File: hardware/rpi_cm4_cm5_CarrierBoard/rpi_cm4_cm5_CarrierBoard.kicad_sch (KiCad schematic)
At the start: 0 parts

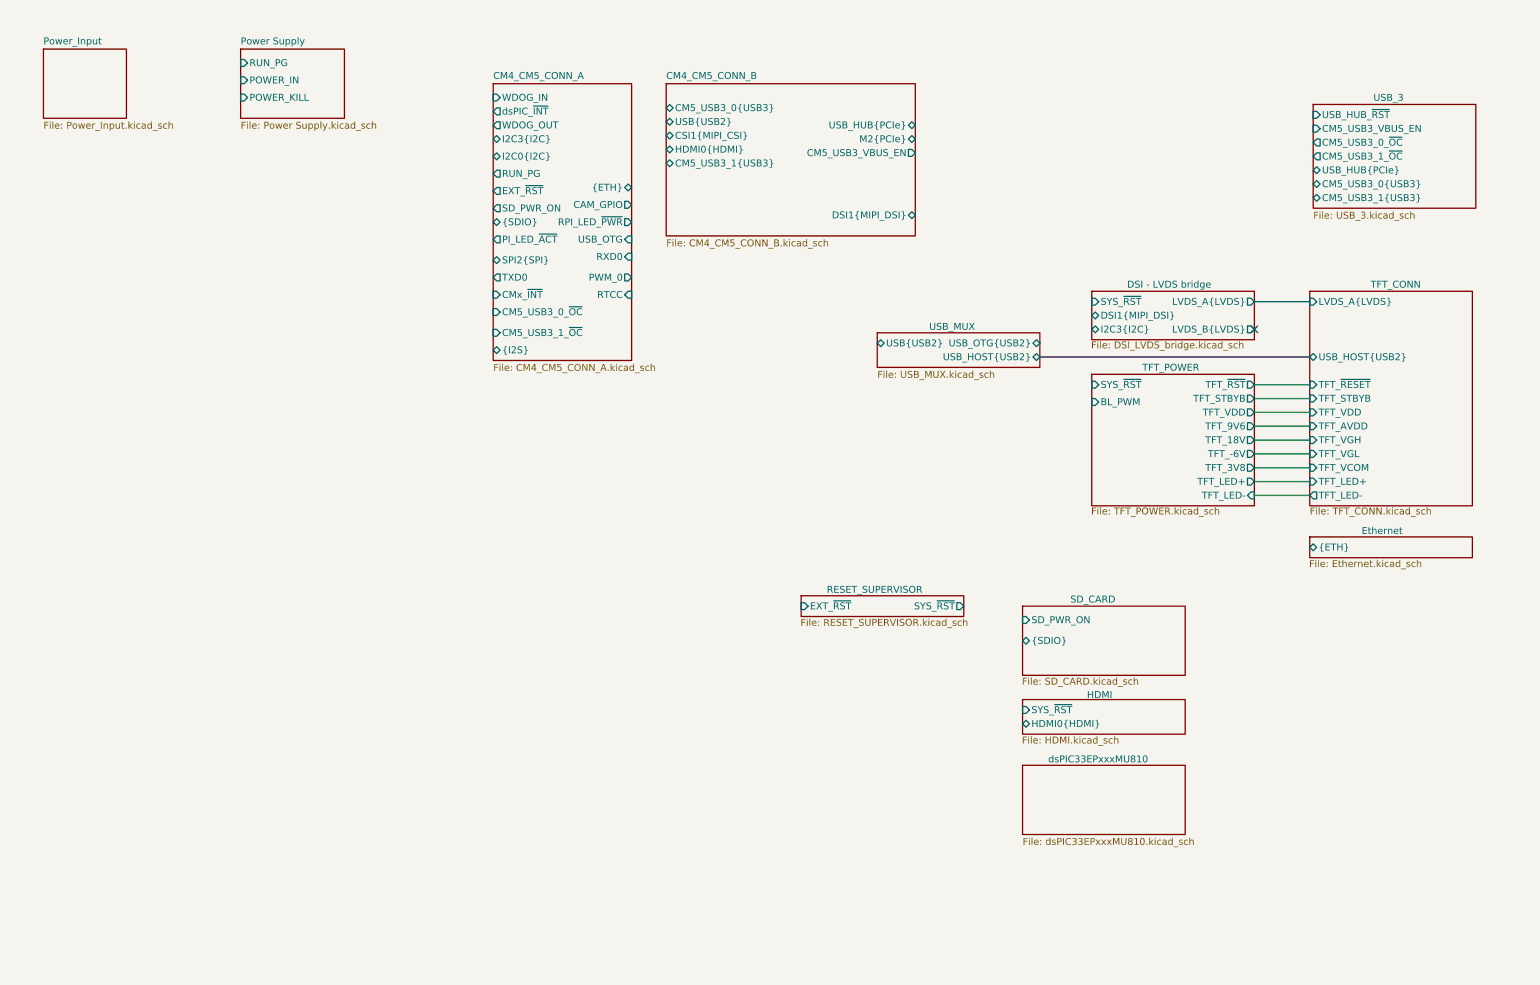
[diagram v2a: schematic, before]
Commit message: Significant update to schematics Add codec, Mikrobus, PIC32A Add power table, design notes for pinmux Add datasheets
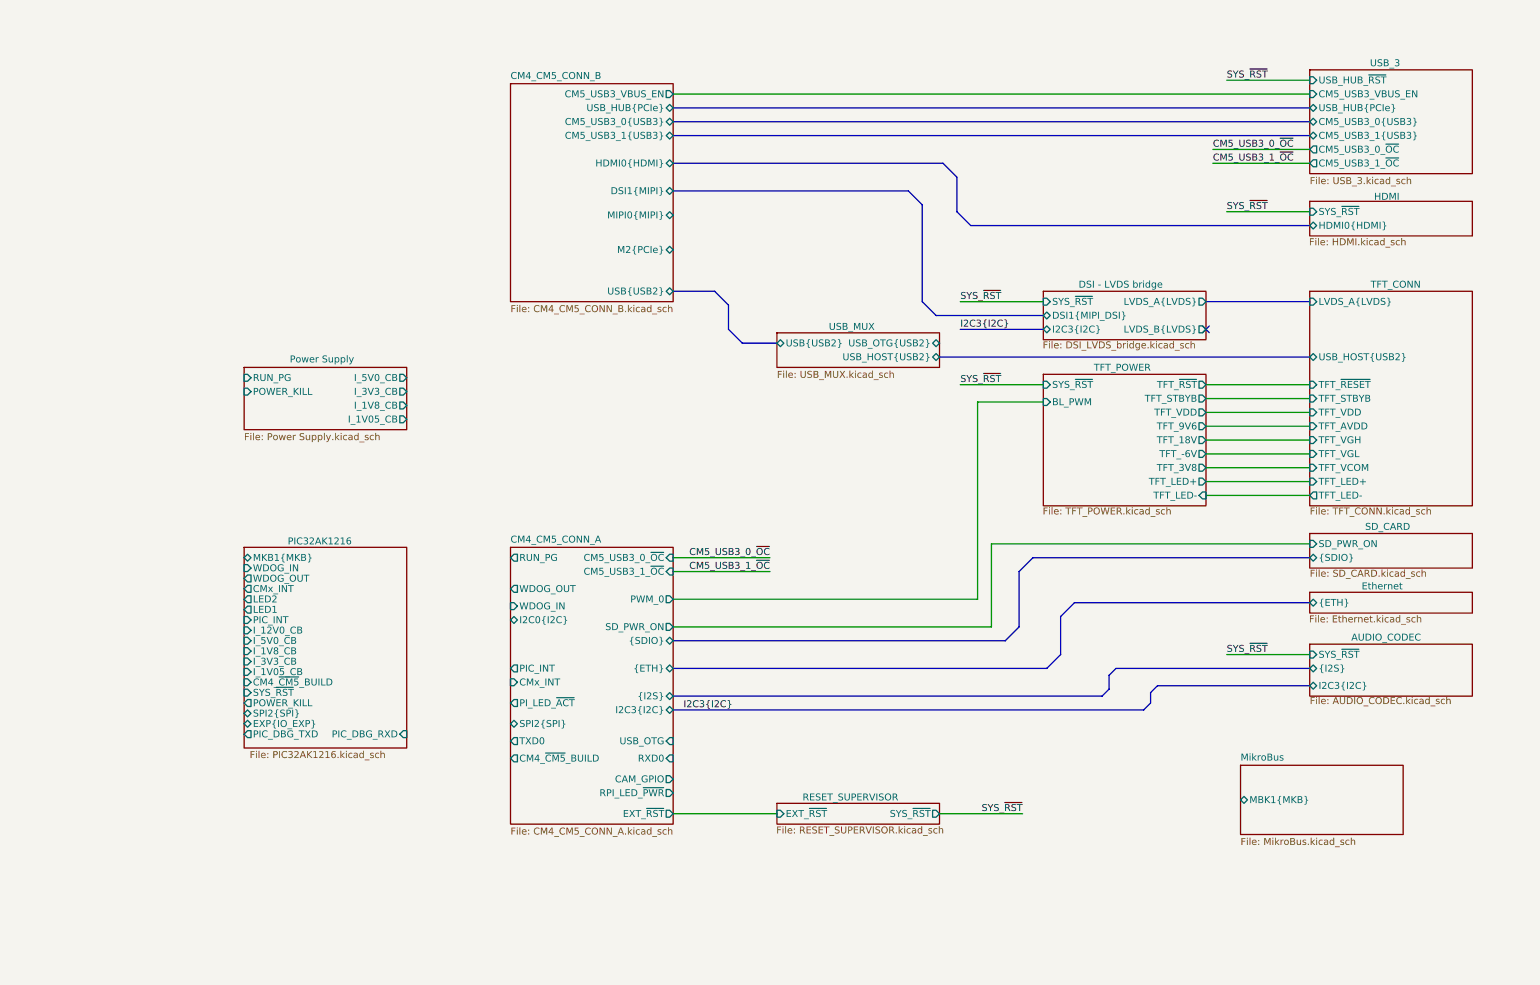
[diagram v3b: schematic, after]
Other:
- sheet dsPIC33EPxxxMU810 renamed PIC32AK1216
- removed sheet Power_Input
- added sheet AUDIO_CODEC (AUDIO_CODEC.kicad_sch)
- added sheet MikroBus (MikroBus.kicad_sch)
- sheet CM4_CM5_CONN_A ports: added CM4_~{CM5}_BUILD, CMx_INT, PIC_INT; removed CMx_~{INT}, RTCC, dsPIC_~{INT}
- sheet CM4_CM5_CONN_B ports: added DSI1{MIPI}, MIPI0{MIPI}; removed CSI1{MIPI_CSI}, DSI1{MIPI_DSI}
- sheet PIC32AK1216: file dsPIC33EPxxxMU810.kicad_sch -> PIC32AK1216.kicad_sch
- sheet PIC32AK1216 ports: added CM4_~{CM5}_BUILD, CMx_INT, EXP{IO_EXP}, I_12V0_CB, I_1V05_CB, I_1V8_CB, I_3V3_CB, I_5V0_CB, LED1, LED2, MKB1{MKB}, PIC_DBG_RXD, PIC_DBG_TXD, PIC_INT, POWER_KILL, SPI2{SPI}, SYS_~{RST}, WDOG_IN, WDOG_OUT; removed none
- sheet Power Supply ports: added I_1V05_CB, I_1V8_CB, I_3V3_CB, I_5V0_CB; removed POWER_IN

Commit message: Slight update to hierarchical top sheet
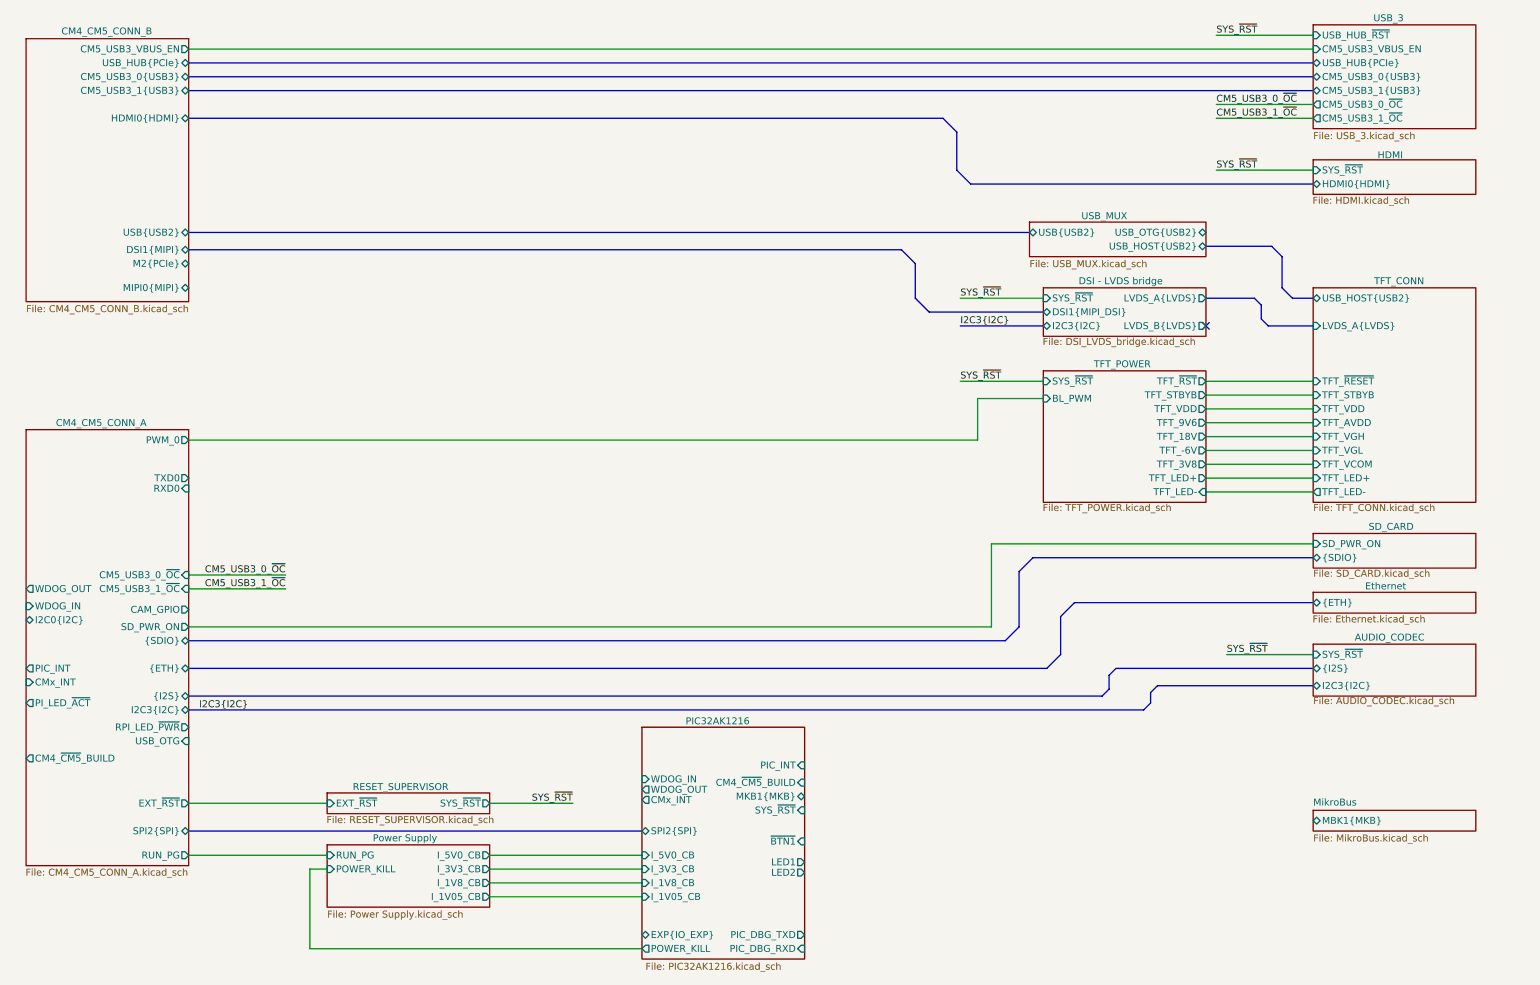
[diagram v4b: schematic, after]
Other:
- sheet PIC32AK1216 ports: added ~{BTN1}; removed I_12V0_CB

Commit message: Preliminary completion of RPI CMx schematics Cleaned up hierarchical root page
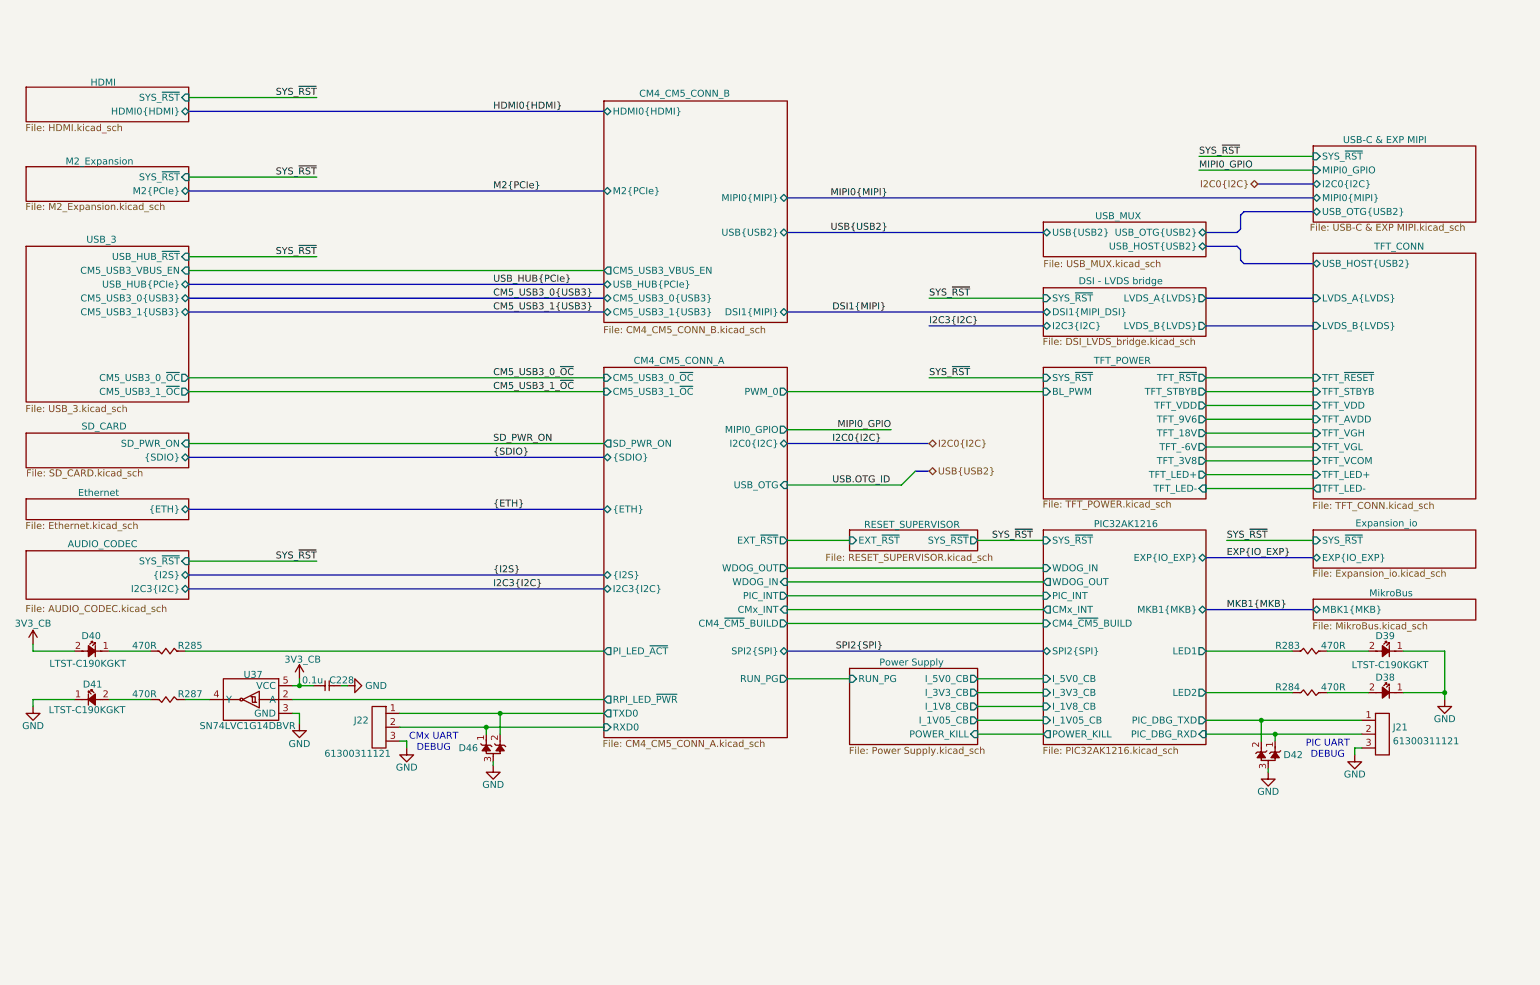
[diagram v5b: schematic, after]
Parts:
- added C228: 0.1u, footprint:CAP_NONPOL_0402, symbol KicadCompDb:Capacitors/CAP_CER_SMT_00001
- added D38, D39, D40, D41: LTST-C190KGKT, footprint:LED_0603, symbol KicadCompDb:Diodes/DIODE_00007
- added D42, D46: D1213A-02SOL-7, footprint:SOT-23-3, symbol KicadCompDb:ESD Diodes/ESD_DIODE_00002
- added J21, J22: 61300311121, footprint:HEADER_3P_2_54MM, symbol KicadCompDb:Connector/CONN_00001
- added R283, R284, R285, R287: 470R, footprint:RES_0402, symbol KicadCompDb:Resistors/RES_SMT_00019
- added U37: SN74LVC1G14DBVR, footprint:SOT-23-5, symbol KicadCompDb:Logic/LOGIC_00003
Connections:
- net CM4_CM5_CONN_A/PI_LED_~{ACT}: now also R285.1
- net CM4_CM5_CONN_A/RPI_LED_~{PWR}: now also U37.2 (A)
- net CM4_CM5_CONN_A/RXD0: now also D46.1, J22.2
- net CM4_CM5_CONN_A/TXD0: now also D46.2 (A), J22.1
- net PIC32AK1216/LED1: now also R283.1
- net PIC32AK1216/LED2: now also R284.1
- net PIC32AK1216/PIC_DBG_RXD: now also D42.1, J21.2
- net PIC32AK1216/PIC_DBG_TXD: now also D42.2 (A), J21.1
- new net: D39.2 (A), R283.2
- new net: D41.2 (A), R287.2
- new net: R287.1, U37.4 (Y)
- new net: D40.1 (K), R285.2
- new net: D38.2 (A), R284.2
- new net 3V3_CB: C228.2, D40.2 (A), U37.5 (VCC)
- new net GND: C228.1, D38.1 (K), D39.1 (K), D41.1 (K), D42.3 (GND), D46.3 (GND), J21.3, J22.3, U37.3 (GND)
- no-connect marks 1 -> 0
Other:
- added sheet Expansion_io (Expansion_io.kicad_sch)
- added sheet M2_Expansion (M2_Expansion.kicad_sch)
- added sheet USB-C & EXP MIPI (USB-C & EXP MIPI.kicad_sch)
- sheet CM4_CM5_CONN_A ports: added MIPI0_GPIO; removed CAM_GPIO
- sheet PIC32AK1216 ports: added none; removed ~{BTN1}
- sheet TFT_CONN ports: added LVDS_B{LVDS}; removed none
- note added: "CMx UART DEBUG"
- note added: "PIC UART DEBUG"

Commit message: Add preliminary BOM and preliminary .pdf schmematics Add BOM option for I2C control of ILI2132A for CapTouch HMI Add BOM options and DNP / 0R resistors for CM4 - CM5 build options
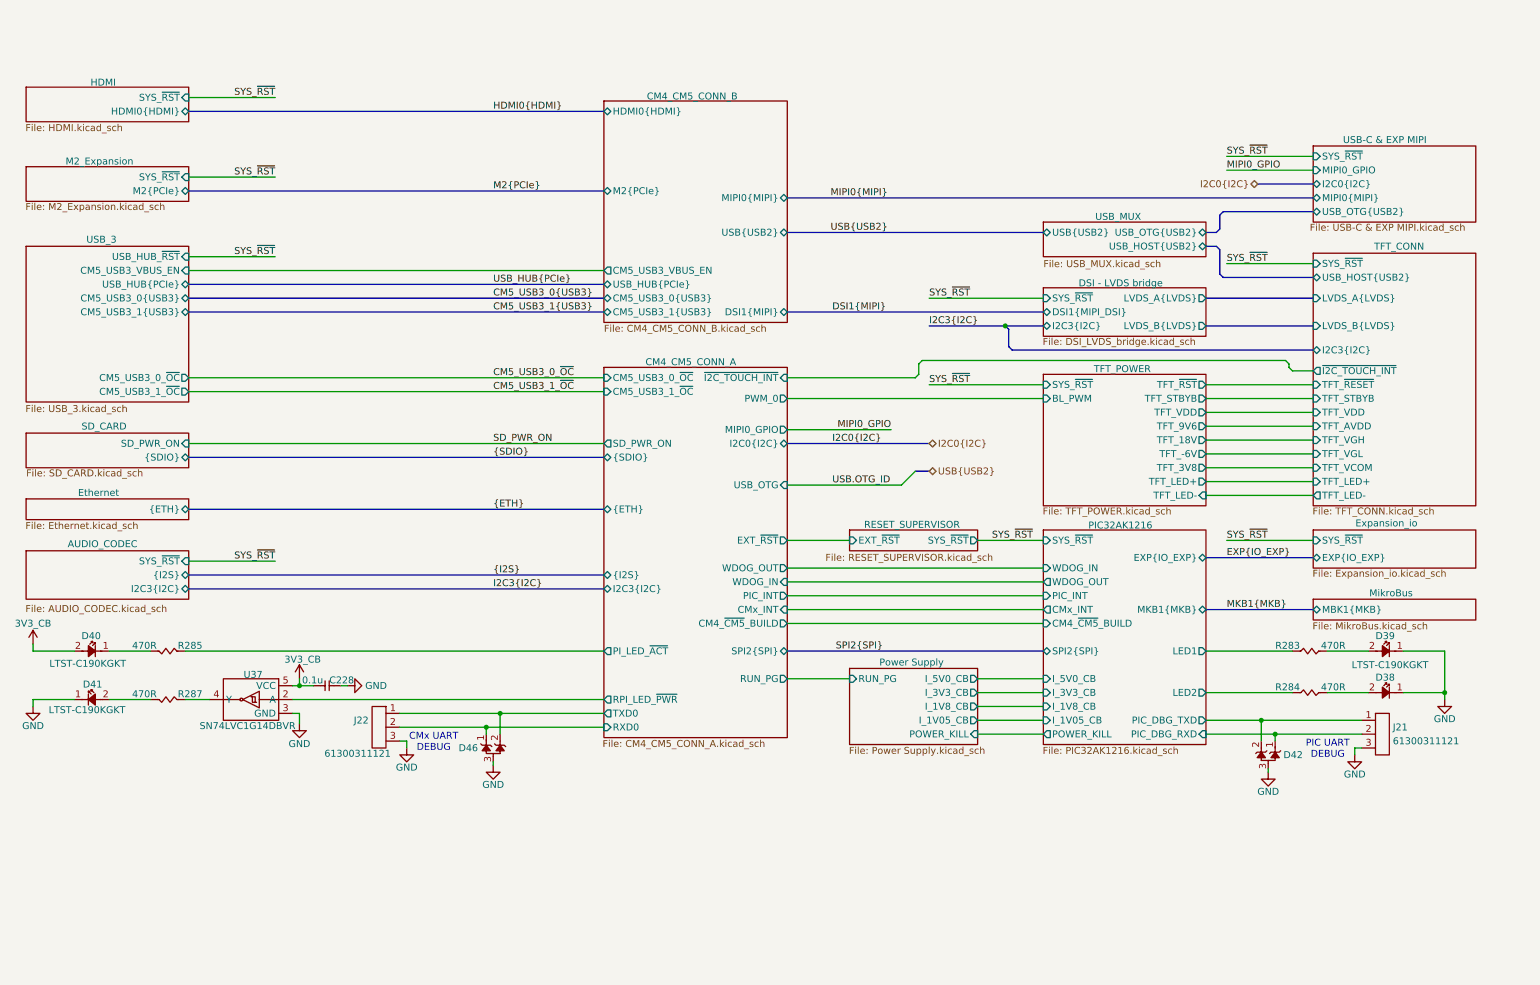
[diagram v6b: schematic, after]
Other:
- sheet CM4_CM5_CONN_A ports: added ~{I2C_TOUCH_INT}; removed none
- sheet TFT_CONN ports: added I2C3{I2C}, SYS_~{RST}, ~{I2C_TOUCH_INT}; removed none
